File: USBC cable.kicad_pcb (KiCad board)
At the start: 2 copper layers, 9.7 x 7.8 mm, 2 parts, among them J1 Conn_01x03, U1 U261-121N-4BS2S

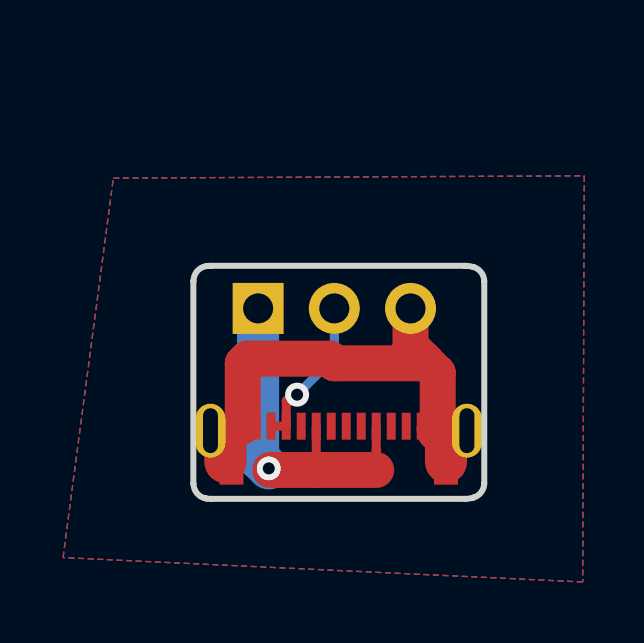
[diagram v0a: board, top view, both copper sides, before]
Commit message: replaced small pins with large pads
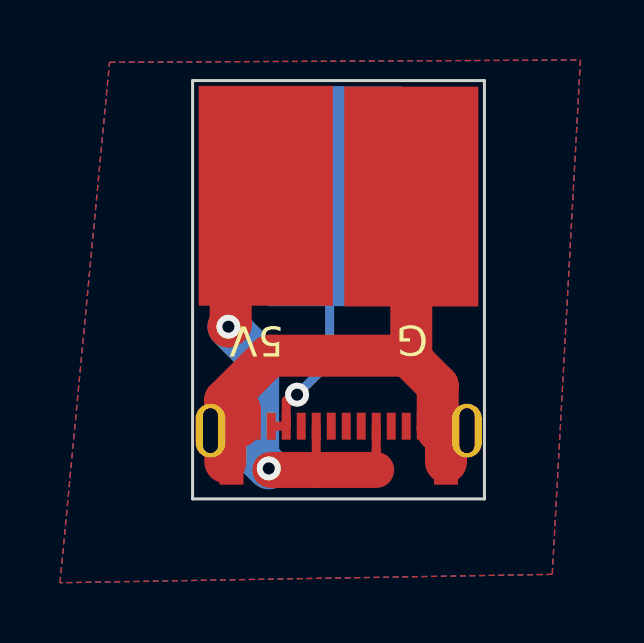
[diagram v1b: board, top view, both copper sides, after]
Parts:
- removed J1: Conn_01x03, Connector_PinHeader_2.54mm:PinHeader_1x03_P2.54mm_Vertical
- added P1: 5V, Connector:CopperField, F.Cu at (129.4, 80.7)
- added P2: GND, Connector:CopperField, F.Cu at (134.3, 80.8)
- added P3: D, Connector:CopperField, B.Cu at (131.9, 80.7)
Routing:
- net GND: track 14.6 -> 19.4 mm
- net +5V: track 12.0 -> 16.7 mm, vias 1 -> 2
- net DATA: track 5.18 -> 8.86 mm
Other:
- board size 9.7 x 7.8 mm -> 9.7 x 13.9 mm
